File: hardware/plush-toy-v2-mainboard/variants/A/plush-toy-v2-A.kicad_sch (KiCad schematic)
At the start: 99 parts, among them U1 ESP32-S3-WROOM-1-N16R8

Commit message: feat(pcb-v2): 版本 A 布线完成，DRC 0 错误 0 未连接
- 网络类收窄（Power 0.6 / Supply 0.4 / Audio 0.3），丝印最小 0.8mm
- In2 改为 VSYS 矩形 + 其余 3V3；电源链按电流走向重排
- IMU SA0 接 3V3（0x19），降压 EN 直连 VSYS
- post_route：网格补线、拉直、快照 --from-snapshot
- route：空 SES 直接失败，非回退只比错误与未连接

Co-Authored-By: Claude Opus 5.5 <noreply@anthropic.com>
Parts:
- removed R_BUCK_EN: 100k, Resistor_SMD:R_0402_1005Metric, symbol Device:R
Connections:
- net BUCK_EN is gone; now on net VSYS: U_BUCK.1 (EN)
- net +3V3: now also U_IMU.3 (SDO/SA0)
- net GND: no longer U_IMU.3 (SDO/SA0)
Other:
- moved on the sheet: C_BUCK_HF, C_BUCK_IN, C_BUCK_OUT1, C_BUCK_OUT2, C_EN, C_FF, C_NTC, C_U1, C_U1_BULK, J_HEAT, J_NTC, L_BUCK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

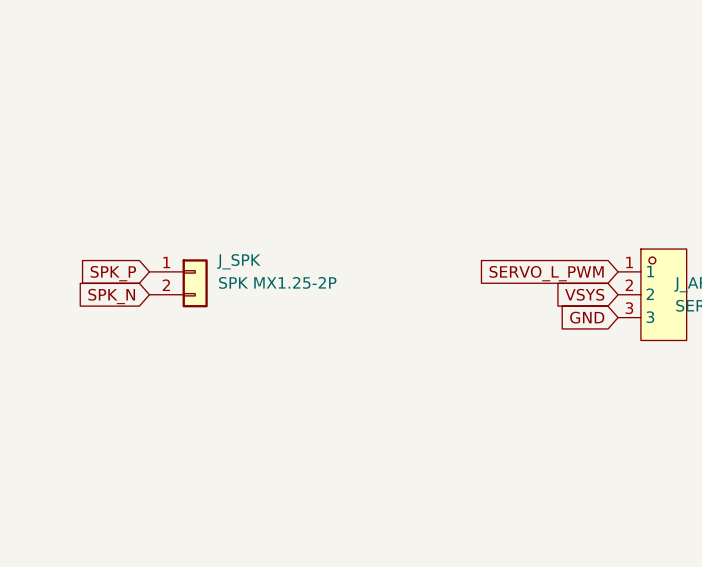
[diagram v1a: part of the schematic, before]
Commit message: feat(pcb-v2): 喇叭座改为 SH1.0 2P，与测温、触摸统一
委托方要求接口规格尽量统一。重新布局布线，DRC 0 错误 0 未连接；
料号 38 种，扩展库 20 种。

Co-Authored-By: Claude Opus 5.5 <noreply@anthropic.com>
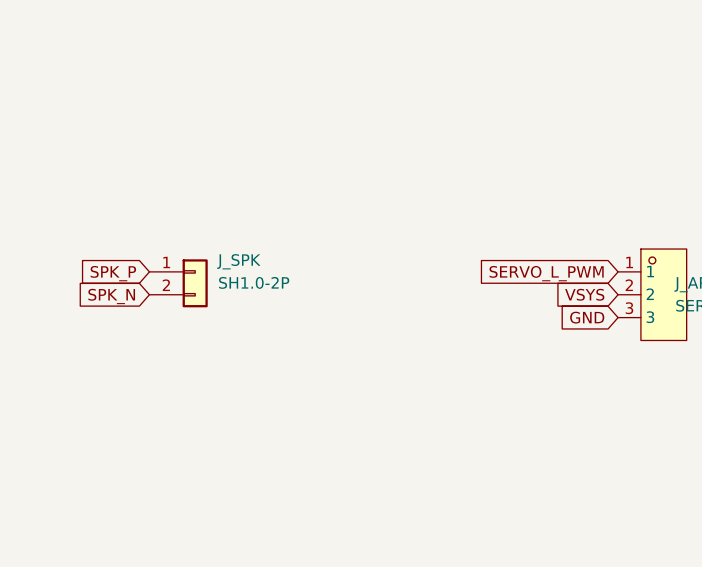
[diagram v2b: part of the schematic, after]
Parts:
- J_SPK: value SPK MX1.25-2P -> SH1.0-2P; footprint Connector_Molex:Molex_PicoBlade_53261-0271_1x02-1MP_P1.25mm_Horizontal -> Connector_JST:JST_SH_SM02B-SRSS-TB_1x02-1MP_P1.00mm_Horizontal; LCSC C177225 -> C160402

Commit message: fix(pcb-v2): 版本 A 去耦布局复查修正，板子加宽到 54×46
复查发现去耦电容只按「附近」放（降压高频电容离引脚 9.9mm、反馈网络 10mm），DRC 查不出。
- 去耦件按引脚就近、同侧放置并加测试（第一颗 ≤3mm，储能 ≤6mm，降压高频电容地焊盘也贴地脚）
- 放置顺序：去耦 → 引脚标注 → 储能电容 → 功能名（长的先排、不得印到邻座旁）→ 其余
- In2 改 VSYS L 形 + 3V3 整层低优先级：降压输出焊盘直接进 3V3 平面，VSYS 不再走细线
- 补线器检查孔距，hole_to_hole 按错误处理；降压热回路表层直连 1.2mm
- 电池座换国产 HX PH2.0-2PWT（C22461285），单板器件费约 $13.1
- 新测试：焊盘间距、功率网络细线、出线座卧式且开口朝板边、功能名归属
- 委托方同意加宽 2mm：54×46mm，一期面积的 46%；DRC 0 错误 0 未连接

Co-Authored-By: Claude Opus 5.5 <noreply@anthropic.com>
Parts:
- J_BAT: footprint Connector_JST:JST_PH_S2B-PH-SM4-TB_1x02-1MP_P2.00mm_Horizontal -> plushv2:CONN-SMD_2P-P2.00_HANXIA_HX-PH2.0-2PWT; LCSC C295747 -> C22461285
